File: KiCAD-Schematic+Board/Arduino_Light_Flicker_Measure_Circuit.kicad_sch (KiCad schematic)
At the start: 42 parts, among them J1 Ds, J2 Ds, J3 FTDI, J4 FTDI-Conn, J5 PWR(5V), J6 USB Power (5V), Q1 BC547, Q2 BC547, U1 ATmega328P-PU, U2 AD5242, U3 AD823A, U4 Display

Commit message: Add new AD5242 symbol recreation for using it as-is and moved some notation to internal symbol library stuff?
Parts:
- U2: symbol PotiDigital_AD5242:AD5242 -> light_flicker_lib:AD5242
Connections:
- net +5V: now also U2.5 (VDD), U2.6 (~{SHDN})
- net GNDD: now also U2.10 (AD1), U2.11 (GND), U2.12 (VSS), U2.9 (AD0)
- net SCL: now also U2.7 (SCL)
- net SDA: now also U2.8 (SDA)
- net at C6.2, J1.3 (Pin_3), U3.6 (-): now also U2.15 (W2), U2.4 (B1)
- net at R4.1: now also U2.3 (W1)
- net at J1.2 (Pin_2): now also U2.14 (B2)
- no-connect marks 25 -> 21
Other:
- note removed: "06.-14. Jan. 2019"
- note removed: "1MΩ"
- note removed: "Light Flicker Detector (Arduino)"
- note removed: "Wolfgang Franke"
- title: (none) -> Light Flicker Detector Arduino
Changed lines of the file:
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@@
 (kicad_sch (version 20230819) (generator eeschema)
   (paper "A4")
+  (title_block
+    (title "Light Flicker Detector Arduino")
+    (date "2023-10-15")
+    (comment 1 "Initially by Wolfgang Franke (https://github.com/WolfgangFranke/LightFlickerMeasure/)")
+    (comment 2 "Updated by Kim C.")
+  )
   (junction (at 260.35 16.51) (diameter 0) (color 0 0 0 0)
   )
@@
   (no_connect (at 119.38 184.15))
   (no_connect (at 69.85 123.19))
-  (no_connect (at 69.85 30.48))
   (no_connect (at 255.27 138.43))
   (no_connect (at 69.85 171.45))
@@
   (no_connect (at 138.43 184.15))
   (no_connect (at 69.85 125.73))
-  (no_connect (at 45.72 34.29))
   (no_connect (at 69.85 166.37))
   (no_connect (at 69.85 176.53))
-  (no_connect (at 45.72 36.83))
-  (no_connect (at 69.85 40.64))
   (no_connect (at 138.43 186.69))
   (no_connect (at 69.85 143.51))
@@
     (stroke (width 0) (type default))
   )
-  (text "1MΩ" (exclude_from_sim no)
- (at 60.96 35.56 0)
-    (effects (font (size 1.27 1.27)))
-  )
   (text "-" (exclude_from_sim no)
  (at 81.28 83.82 0)
@@
     (effects (font (size 1.27 1.27) (thickness 0.254) bold))
   )
-  (text "1MΩ" (exclude_from_sim no)
- (at 60.96 45.72 0)
-    (effects (font (size 1.27 1.27)))
-  )
   (text "+" (exclude_from_sim no)
  (at 81.28 88.9 0)
@@
     (effects (font (size 1.27 1.27) (thickness 0.254) bold))
   )
-  (text "06.-14. Jan. 2019" (exclude_from_sim no)
- (at 204.47 190.5 0)
-    (effects (font (size 1.27 1.27)))
-  )
   (text "Comparator" (exclude_from_sim no)
  (at 182.88 80.645 0)
@@
     (at 90.17 22.225 0)
     (effects (font (size 1.27 1.27)))
-  )
-  (text "Wolfgang Franke" (exclude_from_sim no)
- (at 193.04 175.895 0)
-    (effects (font (size 2.0066 2.0066)))
-  )
-  (text "Light Flicker Detector (Arduino)" (exclude_from_sim no)
- (at 210.82 170.815 0)
-    (effects (font (size 2.4892 2.4892) (thickness 0.4978) bold))
   )
   (text "HighPass 1,5Hz" (exclude_from_sim no)
@@
     )
   )
-  (symbol (lib_id "PotiDigital_AD5242:AD5242") (at 58.42 40.64 0) (unit 1)
-    (exclude_from_sim no) (in_bom yes) (on_board yes) (dnp no)
-    (property "Reference" "U2" (at 57.785 20.8788 0)
-      (effects (font (size 1.27 1.27)))
-    )
-    (property "Value" "AD5242" (at 57.785 23.1902 0)
-      (effects (font (size 1.27 1.27)))
-    )
-    (property "Footprint" "Package_SO:SOIC-16_3.9x9.9mm_P1.27mm" (at 58.42 58.42 0)
-      (effects (font (size 1.27 1.27)) hide)
-    )
-    (property "Datasheet" "http://www.analog.com/media/en/technical-documentation/data-sheets/AD5280_5282.pdf" (at 60.96 43.18 0)
-      (effects (font (size 1.27 1.27)) hide)
-    )
-    (property "Description" "" (at 58.42 40.64 0)
-      (effects (font (size 1.27 1.27)) hide)
-    )
-    (instances
-      (project "Arduino_Light_Flicker_Measure_Circuit"
+  (symbol (lib_id "light_flicker_lib:AD5242") (at 58.42 41.91 0) (unit 1)
+    (exclude_from_sim no) (in_bom yes) (on_board yes) (dnp no)
+    (property "Reference" "U2" (at 49.53 26.67 0)
+      (effects (font (size 1.27 1.27)))
+    )
+    (property "Value" "AD5242" (at 64.135 26.67 0)
+      (effects (font (size 1.27 1.27)))
+    )
+    (property "Footprint" "Package_SO:SOIC-16_3.9x9.9mm_P1.27mm" (at 40.64 64.77 0)
+      (effects (font (size 1.27 1.27) italic) (justify left) hide)
+    )
+    (property "Datasheet" "https://www.analog.com/media/en/technical-documentation/data-sheets/ad5241_5242.pdf" (at 25.4 67.31 0)
+      (effects (font (size 1.27 1.27)) (justify left) hide)
+    )
+    (property "Description" "" (at 52.07 22.86 0)
+      (effects (font (size 1.27 1.27)) hide)
+    )
+    (pin "2")
+    (pin "5")
+    (pin "16")
+    (pin "3")
+    (pin "13")
+    (pin "14")
+    (pin "15")
+    (pin "1")
+    (pin "4")
+    (pin "8")
+    (pin "12")
+    (pin "11")
+    (pin "7")
+    (pin "6")
+    (pin "10")
+    (pin "9")
+    (instances
+      (project "Arduino_Light_Flicker_Measure_Circuit"

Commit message: Add SSD1306 file, minor updates, also swapped two pins.  Slowly iterating.
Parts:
- U4: symbol SSD1306_OLED_I2C:OLED_I2C -> light_flicker_lib:SSD1306; Purchasing (none) -> https://www.amazon.com/UCTRONICS-SSD1306-Self-Luminous-Disp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
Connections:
- net +5V: now also U4.1 (GND), U4.2 (VCC)
- net SCL: now also U4.3 (SCL)
- net SDA: now also U4.4 (SDA)
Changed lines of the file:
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@@
+    (stroke (width 0) (type default))
+  )
+  (wire (pts (xy 148.59 156.21) (xy 149.86 156.21))
     (stroke (width 0) (type default))
   )
@@
   )
   (text " I2C:0x3C" (exclude_from_sim no)
- (at 132.08 140.97 0)
+ (at 136.525 143.51 0)
     (effects (font (size 1.27 1.27)))
   )
@@
     )
   )
-  (symbol (lib_id "SSD1306_OLED_I2C:OLED_I2C") (at 153.67 121.92 0) (mirror y) (unit 1)
-    (exclude_from_sim no) (in_bom yes) (on_board yes) (dnp no)
-    (property "Reference" "U4" (at 140.2588 131.064 0)
-      (effects (font (size 1.27 1.27)) (justify left))
-    )
-    (property "Value" "Display" (at 140.2588 133.3754 0)
-      (effects (font (size 1.27 1.27)) (justify left))
-    )
-    (property "Footprint" "Connector_PinHeader_2.54mm:PinHeader_1x04_P2.54mm_Vertical" (at 154.94 130.81 90)
-      (effects (font (size 1.27 1.27)) hide)
-    )
-    (property "Datasheet" "" (at 154.94 130.81 90)
-      (effects (font (size 1.27 1.27)) hide)
-    )
-    (property "Description" "" (at 153.67 121.92 0)
-      (effects (font (size 1.27 1.27)) hide)
-    )
+  (symbol (lib_id "light_flicker_lib:SSD1306") (at 147.32 137.16 0) (unit 1)
+    (exclude_from_sim no) (in_bom yes) (on_board yes) (dnp no)
+    (property "Reference" "U4" (at 140.97 124.46 0)
+      (effects (font (size 1.27 1.27)) (justify left))
+    )
+    (property "Value" "Display" (at 147.955 124.46 0)
+      (effects (font (size 1.27 1.27)) (justify left))
+    )
+    (property "Footprint" "Connector_PinHeader_2.54mm:PinHeader_1x04_P2.54mm_Vertical" (at 147.32 149.86 0)
+      (effects (font (size 1.27 1.27)) hide)
+    )
+    (property "Datasheet" "https://cdn-shop.adafruit.com/datasheets/SSD1306.pdf" (at 148.59 157.48 0)
+      (effects (font (size 1.27 1.27)) hide)
+    )
+    (property "Description" "128 x 64 Dot Matrix OLED/PLED Segment/Common Driver with Controller " (at 151.13 154.94 0)
+      (effects (font (size 1.27 1.27)) hide)
+    )
+    (property "Purchasing" "https://www.amazon.com/UCTRONICS-SSD1306-Self-Luminous-Display-Raspberry/dp/B072Q2X2LL/ref=sr_1_3?keywords=SSD1306&qid=1697382134&sr=8-3" (at 148.59 152.4 0)
+      (effects (font (size 1.27 1.27)) hide)
+    )
+    (pin "1")
+    (pin "4")
+    (pin "2")
+    (pin "3")
     (instances
       (project "Arduino_Light_Flicker_Measure_Circuit"
@@
         (path "/87ded90a-4f8e-4f0a-a69c-cb4db3584a63"
           (reference "D2") (unit 1)
-        )
-      )
-    )
-  )
-  (symbol (lib_id "power:GNDD") (at 148.59 156.21 0) (unit 1)
-    (exclude_from_sim no) (in_bom yes) (on_board yes) (dnp no)
-    (property "Reference" "#PWR019" (at 148.59 162.56 0)
-      (effects (font (size 1.27 1.27)) hide)
-    )
-    (property "Value" "GNDD" (at 148.6916 160.147 0)
-      (effects (font (size 1.27 1.27)))
-    )
-    (property "Footprint" "" (at 148.59 156.21 0)
-      (effects (font (size 1.27 1.27)) hide)
-    )
-    (property "Datasheet" "" (at 148.59 156.21 0)
-      (effects (font (size 1.27 1.27)) hide)
-    )
-    (property "Description" "" (at 148.59 156.21 0)
-      (effects (font (size 1.27 1.27)) hide)
-    )
-    (pin "1")
-    (instances
-      (project "Arduino_Light_Flicker_Measure_Circuit"
-        (path "/87ded90a-4f8e-4f0a-a69c-cb4db3584a63"
-          (reference "#PWR019") (unit 1)
         )
       )
@@
         )
       )
+    )
+  )
+  (symbol (lib_id "power:+5V") (at 149.86 156.21 0) (unit 1)
+    (exclude_from_sim no) (in_bom yes) (on_board yes) (dnp no)
+    (property "Reference" "#PWR06" (at 149.86 160.02 0)
+      (effects (font (size 1.27 1.27)) hide)
+    )
+    (property "Value" "+5V" (at 150.495 152.4 0)
+      (effects (font (size 1.27 1.27)))
+    )
+    (property "Footprint" "" (at 149.86 156.21 0)
+      (effects (font (size 1.27 1.27)) hide)
+    )
+    (property "Datasheet" "" (at 149.86 156.21 0)
+      (effects (font (size 1.27 1.27)) hide)
+    )
+    (property "Description" "" (at 149.86 156.21 0)
+      (effects (font (size 1.27 1.27)) hide)
+    )
+    (pin "1")
+    (instances
+      (project "Arduino_Light_Flicker_Measure_Circuit"
+        (path "/87ded90a-4f8e-4f0a-a69c-cb4db3584a63"
+          (reference "#PWR06") (unit 1)
+        )
+      )

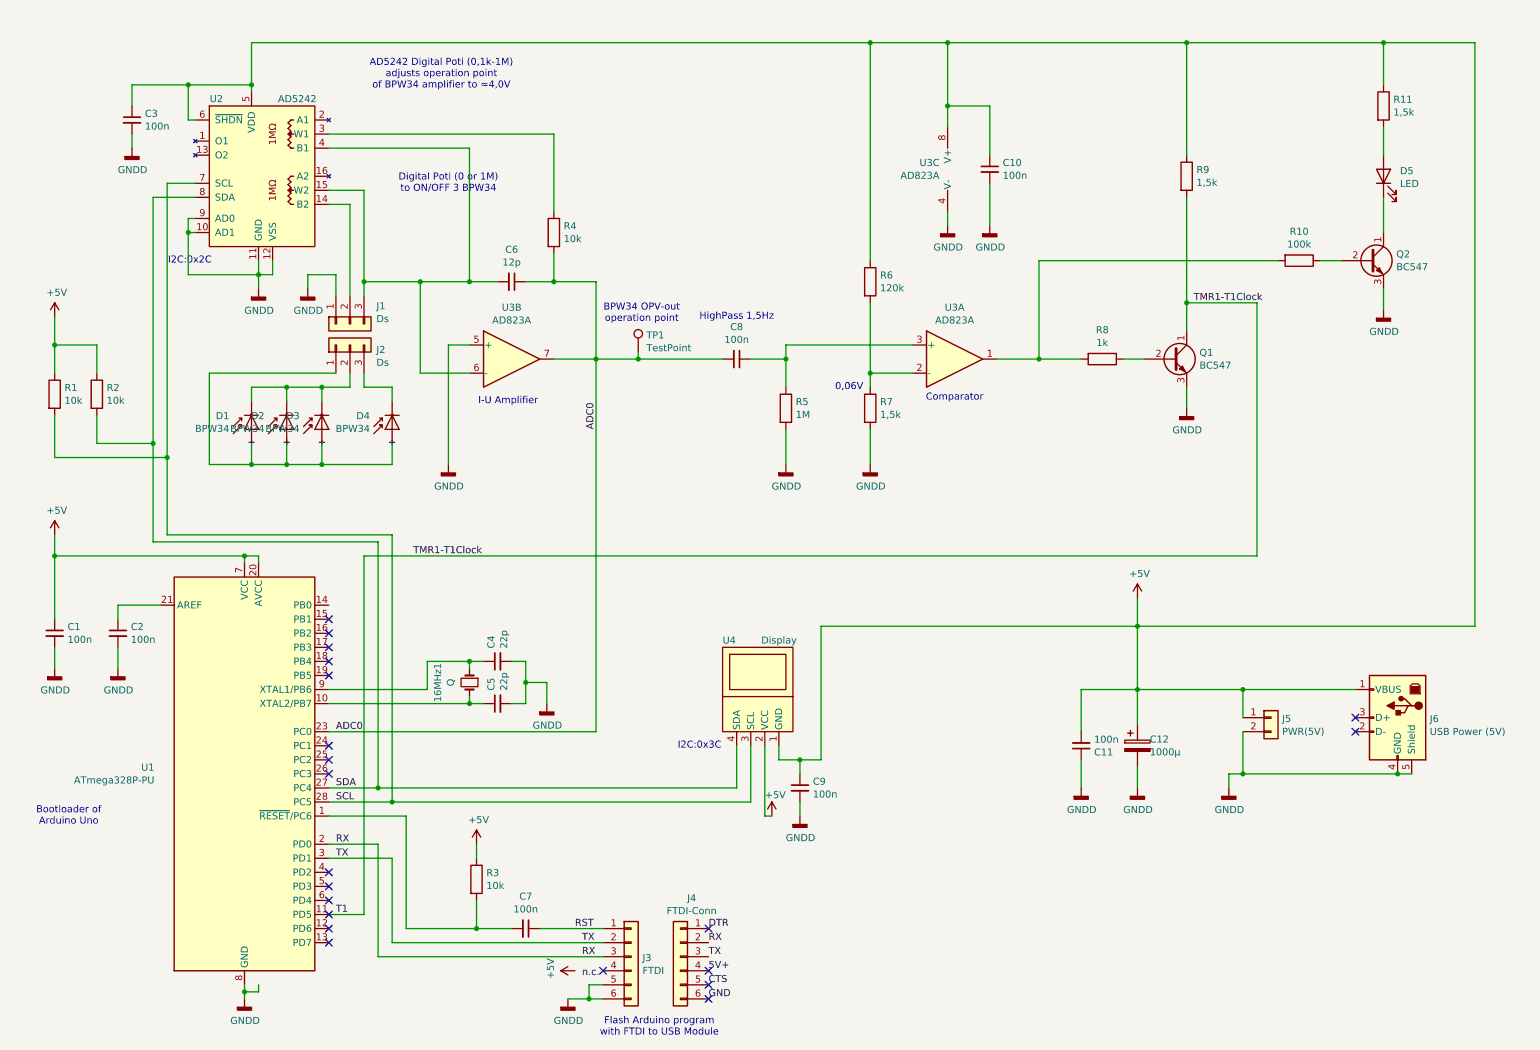
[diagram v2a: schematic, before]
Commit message: Update board setup to be mostly complete.  Still need to shrink and reorganize a bit.
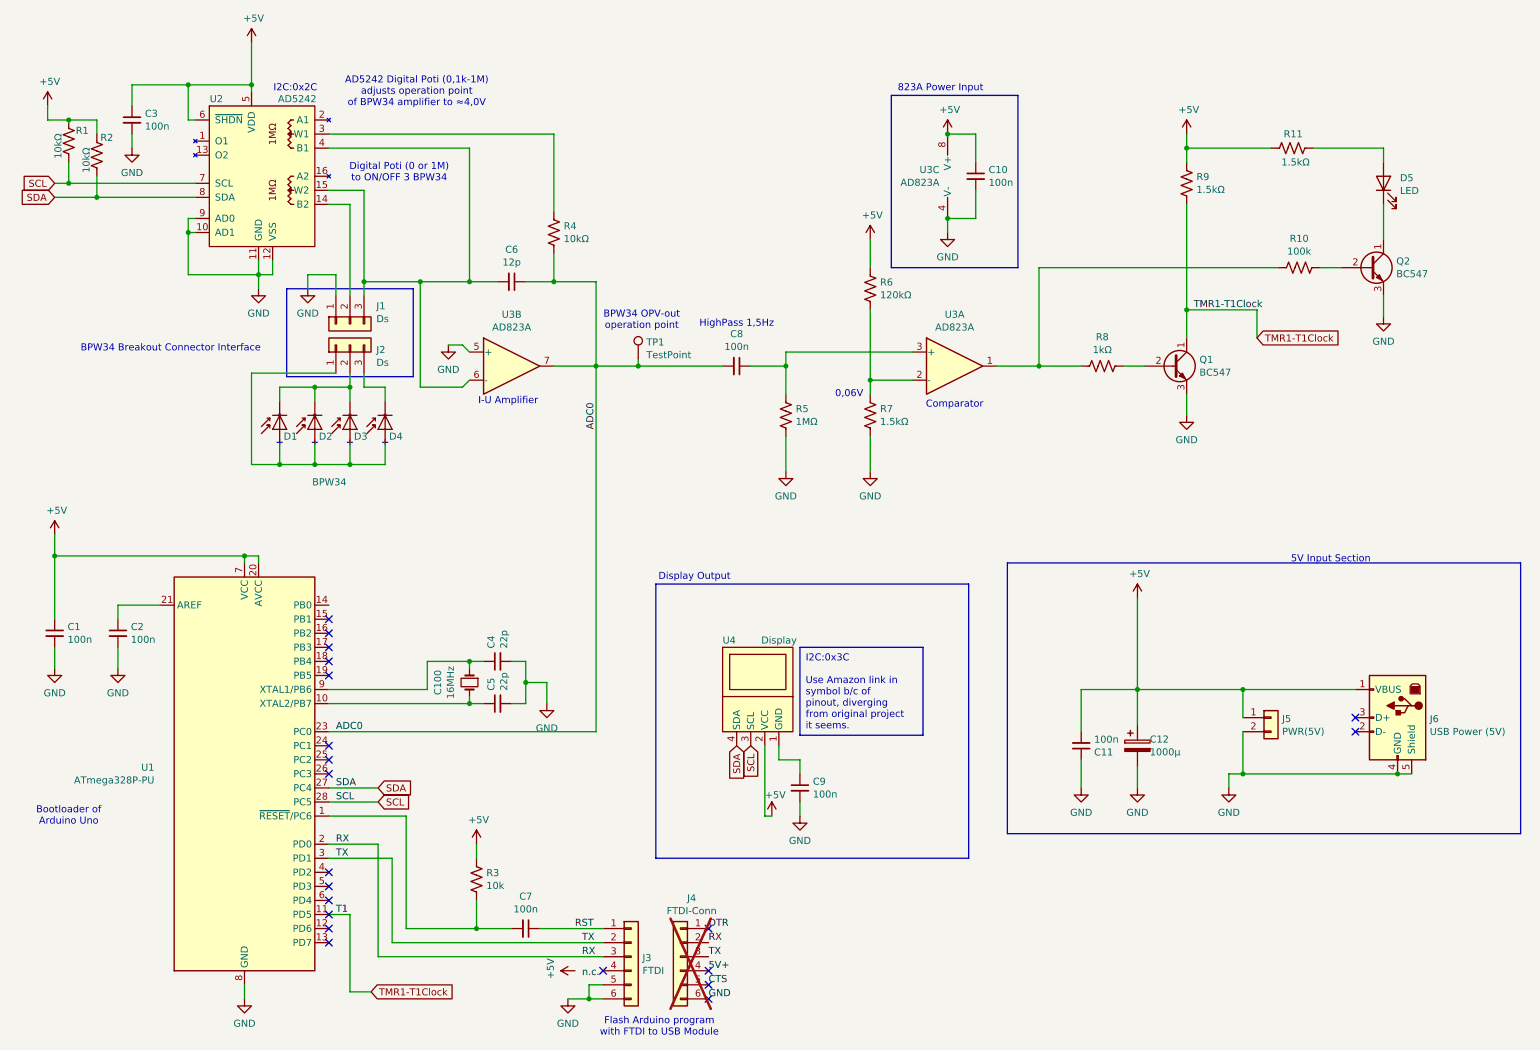
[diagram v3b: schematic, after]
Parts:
- C100: renamed from 16MHz1; value Q -> 16MHz
- J4: now not fitted
- R1, R2: value 10k -> 10kΩ; symbol Device:R -> Device:R_US
- R10, R3: symbol Device:R -> Device:R_US
- R11, R7, R9: value 1,5k -> 1.5kΩ; symbol Device:R -> Device:R_US
- R4: value 10k -> 10kΩ; symbol Device:R -> Device:R_US
- R5: value 1M -> 1MΩ; symbol Device:R -> Device:R_US
- R6: value 120k -> 120kΩ; symbol Device:R -> Device:R_US
- R8: value 1k -> 1kΩ; symbol Device:R -> Device:R_US
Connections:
- net GNDD is gone; now on net GND: C1.2, C10.2, C11.1, C12.2, C2.2, C3.2, C4.2, C5.2, C9.2, J1.1 (Pin_1), J3.5 (Pin_5), J3.6 (Pin_6), J5.2 (Pin_2), J6.4 (GND), J6.5 (Shield), Q1.3 (E), Q2.3 (E), R5.2, R7.2, U1.22 (GND), U1.8 (GND), U2.10 (AD1), U2.11 (GND), U2.12 (VSS), U2.9 (AD0), U3.4 (V-), U3.5 (+)
- net +5V: no longer C9.1, U4.1 (GND)
- net T1 renamed TMR1-T1Clock
- new net: C9.1, U4.1 (GND)
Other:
- note added: "5V Input Section"
- note added: "823A Power Input"
- note added: "BPW34 Breakout Connector Interface"
- note added: "Display Output"
- note removed: "I2C:0x3C"
- moved on the sheet: C10, C8, D1, D2, D3, D4, D5, Q1, Q2, TP1, U3A, U3B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

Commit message: Fix broken gitignore due to typo... Ouch.  Also clean up schematic even more, still need to do proper layout and BOM sourcing stuff.  Plus figure out the actual parts for the photodiodes still.
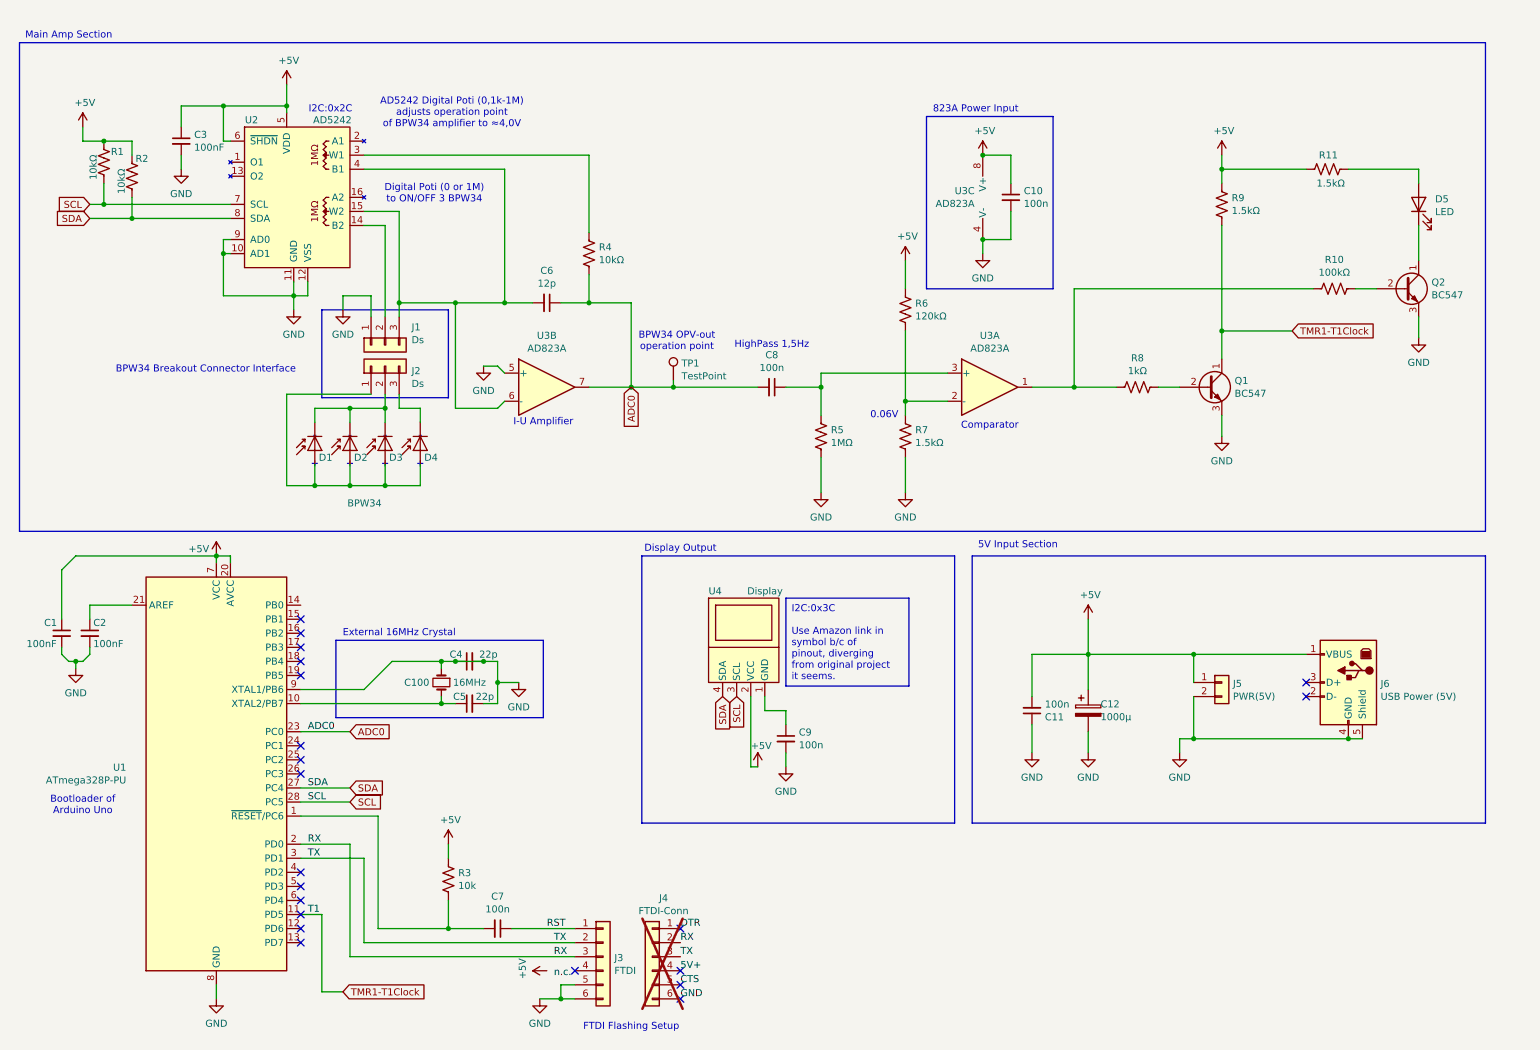
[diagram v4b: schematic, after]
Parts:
- C1, C2, C3: value 100n -> 100nF
- R10: value 100k -> 100kΩ
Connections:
- net GND: now also C100.1, C4.1, U1.9 (XTAL1/PB6)
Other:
- note added: "0.06V"
- note added: "External 16MHz Crystal"
- note added: "FTDI Flashing Setup"
- note added: "Main Amp Section"
- note removed: "0,06V"
- note removed: "Flash Arduino program with FTDI to USB Module"
- moved on the sheet: C1, C10, C100, C11, C12, C2, C3, C4, C5, C6, C7, C8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
